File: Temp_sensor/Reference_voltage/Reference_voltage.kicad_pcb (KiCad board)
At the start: 2 copper layers, 100 x 100 mm, 58 parts, among them J1 CN3, J2 CN4, SW1 SW_DIP_x01, SW2 SW_DIP_x01, U1 HDSP-7401_Paulo, U2 HDSP-7401_Paulo, U3 HDSP-7401_Paulo, U4 HDSP-7401_Paulo, U5 LM4128, U6 74HC595, U7 74HC595, U8 74HC595, U9 74HC595

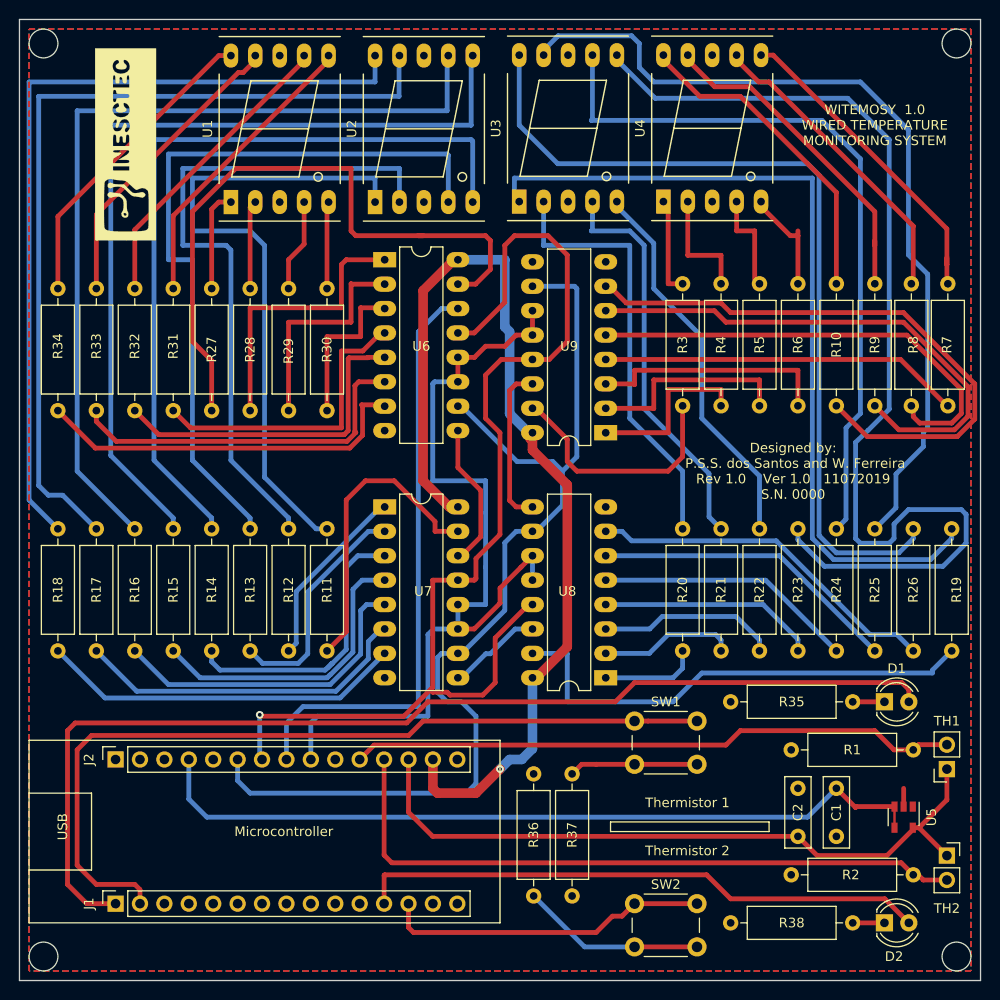
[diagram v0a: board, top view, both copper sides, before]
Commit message: Through Hole to SMD components
first print of the board
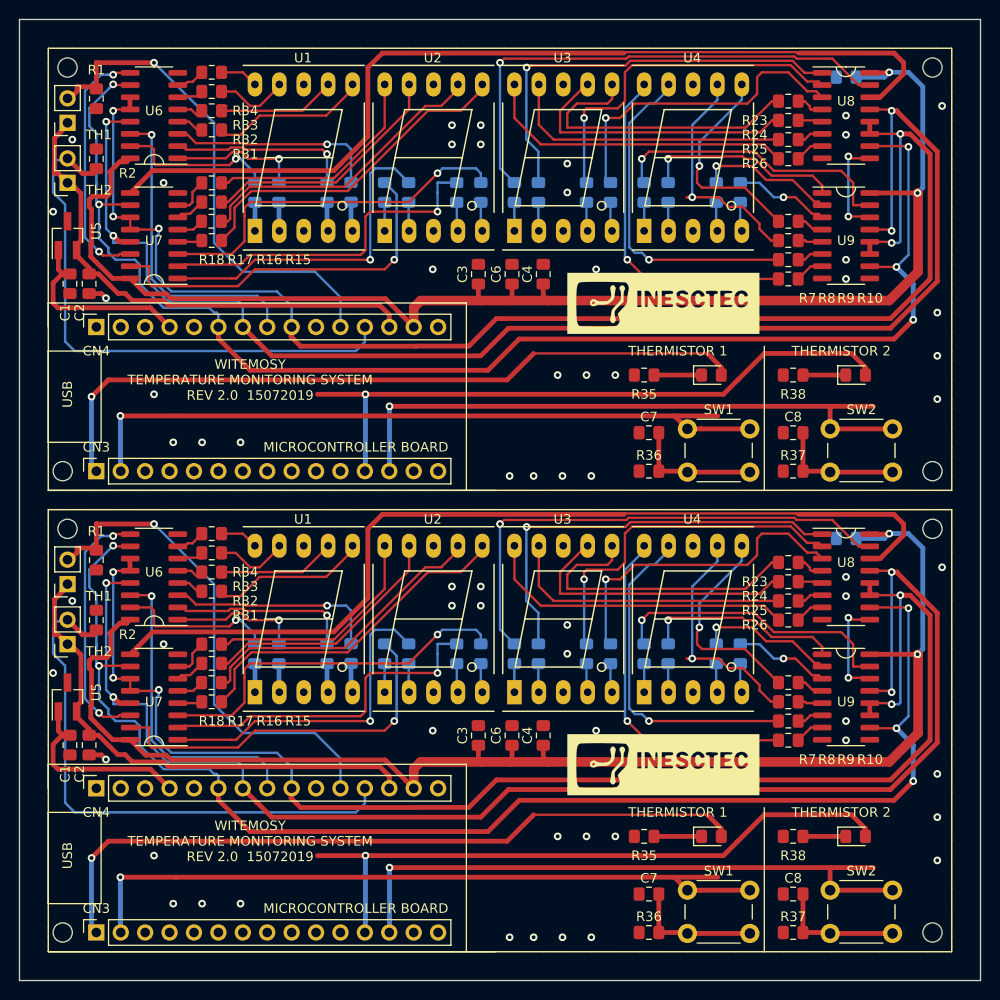
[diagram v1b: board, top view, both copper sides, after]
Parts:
- removed the C1 at (180.0, 125.0)
- removed the C2 at (176.0, 130.0)
- removed D1, D2: LED, LED_THT:LED_D4.0mm
- removed the G*** at (106.0, 58.0)
- removed J1: CN3, Connector_PinSocket_2.54mm:PinSocket_1x15_P2.54mm_Vertical
- removed J2: CN4, Connector_PinSocket_2.54mm:PinSocket_1x15_P2.54mm_Vertical
- removed the R1 at (188.0, 121.0)
- removed the R10 at (180.0, 72.5)
- removed the R11 at (127.0, 98.0)
- removed the R12 at (123.0, 98.0)
- removed the R13 at (119.0, 98.0)
- removed the R14 at (115.0, 98.0)
- removed the R15 at (111.0, 98.0)
- removed the R16 at (107.0, 98.0)
- removed the R17 at (103.0, 98.0)
- removed the R18 at (99.0, 98.0)
- removed the R19 at (192.0, 98.0)
- removed the R2 at (188.0, 134.0)
- removed the R20 at (164.0, 98.0)
- removed the R21 at (168.0, 98.0)
- removed the R22 at (172.0, 98.0)
- removed the R23 at (176.0, 98.0)
- removed the R24 at (180.0, 98.0)
- removed the R25 at (184.0, 98.0)
- removed the R26 at (188.0, 98.0)
- removed the R27 at (115.0, 73.0)
- removed the R28 at (119.0, 73.0)
- removed the R29 at (123.0, 73.0)
- removed the R3 at (164.0, 72.5)
- removed the R30 at (127.0, 73.0)
- removed the R31 at (111.0, 73.0)
- removed the R32 at (107.0, 73.0)
- removed the R33 at (103.0, 73.0)
- removed the R34 at (99.0, 73.0)
- removed the R35 at (169.0, 116.0)
- removed the R36 at (152.5, 136.2)
- removed the R37 at (148.5, 123.5)
- removed the R38 at (169.0, 139.0)
- removed the R4 at (168.0, 72.5)
- removed the R5 at (172.0, 72.5)
- removed the R6 at (176.0, 72.5)
- removed the R7 at (191.6, 72.5)
- removed the R8 at (187.8, 72.5)
- removed the R9 at (184.0, 72.5)
- removed the SW1 at (159.0, 118.0)
- removed the SW2 at (159.0, 137.0)
- removed the TH1 at (191.5, 123.0)
- removed the TH2 at (191.5, 132.0)
- removed the U1 at (117.0, 64.0)
- removed the U2 at (132.0, 64.0)
- removed the U3 at (147.0, 64.0)
- removed the U4 at (162.0, 64.0)
- removed the U5 at (187.0, 128.0)
- removed the U6 at (133.0, 70.0)
- removed the U7 at (133.0, 95.7)
- removed the U8 at (156.0, 113.5)
- removed the U9 at (156.0, 88.0)
- added C1: 100n, Capacitor_SMD:C_0805_2012Metric_Pad1.15x1.40mm_HandSolder, F.Cu at (100.2, 120.5)
- added C1: 100n, Capacitor_SMD:C_0805_2012Metric_Pad1.15x1.40mm_HandSolder, F.Cu at (100.2, 72.5)
- added C2: 100n, Capacitor_SMD:C_0805_2012Metric_Pad1.15x1.40mm_HandSolder, F.Cu at (102.2, 120.5)
- added C2: 100n, Capacitor_SMD:C_0805_2012Metric_Pad1.15x1.40mm_HandSolder, F.Cu at (102.2, 72.5)
- added C3: 100n, Capacitor_SMD:C_0805_2012Metric_Pad1.15x1.40mm_HandSolder, F.Cu at (142.8, 119.5)
- added C3: 100n, Capacitor_SMD:C_0805_2012Metric_Pad1.15x1.40mm_HandSolder, F.Cu at (142.8, 71.5)
- added C4: 100n, Capacitor_SMD:C_0805_2012Metric_Pad1.15x1.40mm_HandSolder, F.Cu at (149.5, 119.5)
- added C4: 100n, Capacitor_SMD:C_0805_2012Metric_Pad1.15x1.40mm_HandSolder, F.Cu at (149.5, 71.5)
- added C5: 100n, Capacitor_SMD:C_0805_2012Metric_Pad1.15x1.40mm_HandSolder, B.Cu at (181.0, 99.0)
- added C5: 100n, Capacitor_SMD:C_0805_2012Metric_Pad1.15x1.40mm_HandSolder, B.Cu at (181.0, 51.0)
- added C6: 100n, Capacitor_SMD:C_0805_2012Metric_Pad1.15x1.40mm_HandSolder, F.Cu at (146.2, 119.5)
- added C6: 100n, Capacitor_SMD:C_0805_2012Metric_Pad1.15x1.40mm_HandSolder, F.Cu at (146.2, 71.5)
- added C7: 100n, Capacitor_SMD:C_0805_2012Metric_Pad1.15x1.40mm_HandSolder, F.Cu at (160.5, 136.0)
- added C7: 100n, Capacitor_SMD:C_0805_2012Metric_Pad1.15x1.40mm_HandSolder, F.Cu at (160.5, 88.0)
- added C8: 100n, Capacitor_SMD:C_0805_2012Metric_Pad1.15x1.40mm_HandSolder, F.Cu at (175.5, 136.0)
- added C8: 100n, Capacitor_SMD:C_0805_2012Metric_Pad1.15x1.40mm_HandSolder, F.Cu at (175.5, 88.0)
- added CN3: CN3, Connector_PinSocket_2.54mm:PinSocket_1x15_P2.54mm_Vertical, F.Cu at (103.0, 140.0)
- added CN3: CN3, Connector_PinSocket_2.54mm:PinSocket_1x15_P2.54mm_Vertical, F.Cu at (103.0, 92.0)
- added CN4: CN4, Connector_PinSocket_2.54mm:PinSocket_1x15_P2.54mm_Vertical, F.Cu at (103.0, 125.0)
- added CN4: CN4, Connector_PinSocket_2.54mm:PinSocket_1x15_P2.54mm_Vertical, F.Cu at (103.0, 77.0)
- added G***: LOGO, Documents:logoinesc4, F.Cu at (162.0, 122.5)
- added G***: LOGO, Documents:logoinesc4, F.Cu at (162.0, 74.5)
- added ON: LED, LED_SMD:LED_0805_2012Metric_Pad1.15x1.40mm_HandSolder, F.Cu at (182.0, 130.0)
- added ON: LED, LED_SMD:LED_0805_2012Metric_Pad1.15x1.40mm_HandSolder, F.Cu at (167.0, 130.0)
- added ON: LED, LED_SMD:LED_0805_2012Metric_Pad1.15x1.40mm_HandSolder, F.Cu at (182.0, 82.0)
- added ON: LED, LED_SMD:LED_0805_2012Metric_Pad1.15x1.40mm_HandSolder, F.Cu at (167.0, 82.0)
- added R1: 10k, Resistor_SMD:R_0805_2012Metric_Pad1.15x1.40mm_HandSolder, F.Cu at (103.0, 101.2)
- added R1: 10k, Resistor_SMD:R_0805_2012Metric_Pad1.15x1.40mm_HandSolder, F.Cu at (103.0, 53.2)
- added R10: 560, Resistor_SMD:R_0805_2012Metric_Pad1.15x1.40mm_HandSolder, F.Cu at (175.0, 120.0)
- added R10: 560, Resistor_SMD:R_0805_2012Metric_Pad1.15x1.40mm_HandSolder, F.Cu at (175.0, 72.0)
- added R11: 560, Resistor_SMD:R_0805_2012Metric_Pad1.15x1.40mm_HandSolder, B.Cu at (133.0, 111.0)
- added R11: 560, Resistor_SMD:R_0805_2012Metric_Pad1.15x1.40mm_HandSolder, B.Cu at (133.0, 63.0)
- added R12: 560, Resistor_SMD:R_0805_2012Metric_Pad1.15x1.40mm_HandSolder, B.Cu at (135.5, 111.0)
- added R12: 560, Resistor_SMD:R_0805_2012Metric_Pad1.15x1.40mm_HandSolder, B.Cu at (135.5, 63.0)
- added R13: 560, Resistor_SMD:R_0805_2012Metric_Pad1.15x1.40mm_HandSolder, B.Cu at (140.5, 111.0)
- added R13: 560, Resistor_SMD:R_0805_2012Metric_Pad1.15x1.40mm_HandSolder, B.Cu at (140.5, 63.0)
- added R14: 560, Resistor_SMD:R_0805_2012Metric_Pad1.15x1.40mm_HandSolder, B.Cu at (143.0, 111.0)
- added R14: 560, Resistor_SMD:R_0805_2012Metric_Pad1.15x1.40mm_HandSolder, B.Cu at (143.0, 63.0)
- added R15: 560, Resistor_SMD:R_0805_2012Metric_Pad1.15x1.40mm_HandSolder, F.Cu at (115.0, 116.0)
- added R15: 560, Resistor_SMD:R_0805_2012Metric_Pad1.15x1.40mm_HandSolder, F.Cu at (115.0, 68.0)
- added R16: 560, Resistor_SMD:R_0805_2012Metric_Pad1.15x1.40mm_HandSolder, F.Cu at (115.0, 114.0)
- added R16: 560, Resistor_SMD:R_0805_2012Metric_Pad1.15x1.40mm_HandSolder, F.Cu at (115.0, 66.0)
- added R17: 560, Resistor_SMD:R_0805_2012Metric_Pad1.15x1.40mm_HandSolder, F.Cu at (115.0, 112.0)
- added R17: 560, Resistor_SMD:R_0805_2012Metric_Pad1.15x1.40mm_HandSolder, F.Cu at (115.0, 64.0)
- added R18: 560, Resistor_SMD:R_0805_2012Metric_Pad1.15x1.40mm_HandSolder, F.Cu at (115.0, 110.0)
- added R18: 560, Resistor_SMD:R_0805_2012Metric_Pad1.15x1.40mm_HandSolder, F.Cu at (115.0, 62.0)
- added R19: 560, Resistor_SMD:R_0805_2012Metric_Pad1.15x1.40mm_HandSolder, B.Cu at (146.5, 111.0)
- added R19: 560, Resistor_SMD:R_0805_2012Metric_Pad1.15x1.40mm_HandSolder, B.Cu at (146.5, 63.0)
- added R2: 10k, Resistor_SMD:R_0805_2012Metric_Pad1.15x1.40mm_HandSolder, F.Cu at (103.0, 107.5)
- added R2: 10k, Resistor_SMD:R_0805_2012Metric_Pad1.15x1.40mm_HandSolder, F.Cu at (103.0, 59.5)
- added R20: 560, Resistor_SMD:R_0805_2012Metric_Pad1.15x1.40mm_HandSolder, B.Cu at (149.0, 111.0)
- added R20: 560, Resistor_SMD:R_0805_2012Metric_Pad1.15x1.40mm_HandSolder, B.Cu at (149.0, 63.0)
- added R21: 560, Resistor_SMD:R_0805_2012Metric_Pad1.15x1.40mm_HandSolder, B.Cu at (154.0, 111.0)
- added R21: 560, Resistor_SMD:R_0805_2012Metric_Pad1.15x1.40mm_HandSolder, B.Cu at (154.0, 63.0)
- added R22: 560, Resistor_SMD:R_0805_2012Metric_Pad1.15x1.40mm_HandSolder, B.Cu at (156.5, 111.0)
- added R22: 560, Resistor_SMD:R_0805_2012Metric_Pad1.15x1.40mm_HandSolder, B.Cu at (156.5, 63.0)
- added R23: 560, Resistor_SMD:R_0805_2012Metric_Pad1.15x1.40mm_HandSolder, F.Cu at (175.0, 101.5)
- added R23: 560, Resistor_SMD:R_0805_2012Metric_Pad1.15x1.40mm_HandSolder, F.Cu at (175.0, 53.5)
- added R24: 560, Resistor_SMD:R_0805_2012Metric_Pad1.15x1.40mm_HandSolder, F.Cu at (175.0, 103.5)
- added R24: 560, Resistor_SMD:R_0805_2012Metric_Pad1.15x1.40mm_HandSolder, F.Cu at (175.0, 55.5)
- added R25: 560, Resistor_SMD:R_0805_2012Metric_Pad1.15x1.40mm_HandSolder, F.Cu at (175.0, 105.5)
- added R25: 560, Resistor_SMD:R_0805_2012Metric_Pad1.15x1.40mm_HandSolder, F.Cu at (175.0, 57.5)
- added R26: 560, Resistor_SMD:R_0805_2012Metric_Pad1.15x1.40mm_HandSolder, F.Cu at (175.0, 107.5)
- added R26: 560, Resistor_SMD:R_0805_2012Metric_Pad1.15x1.40mm_HandSolder, F.Cu at (175.0, 59.5)
- added R27: 560, Resistor_SMD:R_0805_2012Metric_Pad1.15x1.40mm_HandSolder, B.Cu at (119.5, 111.0)
- added R27: 560, Resistor_SMD:R_0805_2012Metric_Pad1.15x1.40mm_HandSolder, B.Cu at (119.5, 63.0)
- added R28: 560, Resistor_SMD:R_0805_2012Metric_Pad1.15x1.40mm_HandSolder, B.Cu at (122.0, 111.0)
- added R28: 560, Resistor_SMD:R_0805_2012Metric_Pad1.15x1.40mm_HandSolder, B.Cu at (122.0, 63.0)
- added R29: 560, Resistor_SMD:R_0805_2012Metric_Pad1.15x1.40mm_HandSolder, B.Cu at (127.0, 111.0)
- added R29: 560, Resistor_SMD:R_0805_2012Metric_Pad1.15x1.40mm_HandSolder, B.Cu at (127.0, 63.0)
- added R3: 560, Resistor_SMD:R_0805_2012Metric_Pad1.15x1.40mm_HandSolder, B.Cu at (160.0, 111.0)
- added R3: 560, Resistor_SMD:R_0805_2012Metric_Pad1.15x1.40mm_HandSolder, B.Cu at (160.0, 63.0)
- added R30: 560, Resistor_SMD:R_0805_2012Metric_Pad1.15x1.40mm_HandSolder, B.Cu at (129.5, 111.0)
- added R30: 560, Resistor_SMD:R_0805_2012Metric_Pad1.15x1.40mm_HandSolder, B.Cu at (129.5, 63.0)
- added R31: 560, Resistor_SMD:R_0805_2012Metric_Pad1.15x1.40mm_HandSolder, F.Cu at (115.0, 104.5)
- added R31: 560, Resistor_SMD:R_0805_2012Metric_Pad1.15x1.40mm_HandSolder, F.Cu at (115.0, 56.5)
- added R32: 560, Resistor_SMD:R_0805_2012Metric_Pad1.15x1.40mm_HandSolder, F.Cu at (115.0, 102.5)
- added R32: 560, Resistor_SMD:R_0805_2012Metric_Pad1.15x1.40mm_HandSolder, F.Cu at (115.0, 54.5)
- added R33: 560, Resistor_SMD:R_0805_2012Metric_Pad1.15x1.40mm_HandSolder, F.Cu at (115.0, 100.5)
- added R33: 560, Resistor_SMD:R_0805_2012Metric_Pad1.15x1.40mm_HandSolder, F.Cu at (115.0, 52.5)
- added R34: 560, Resistor_SMD:R_0805_2012Metric_Pad1.15x1.40mm_HandSolder, F.Cu at (115.0, 98.5)
- added R34: 560, Resistor_SMD:R_0805_2012Metric_Pad1.15x1.40mm_HandSolder, F.Cu at (115.0, 50.5)
- added R35: 220, Resistor_SMD:R_0805_2012Metric_Pad1.15x1.40mm_HandSolder, F.Cu at (160.0, 130.0)
- added R35: 220, Resistor_SMD:R_0805_2012Metric_Pad1.15x1.40mm_HandSolder, F.Cu at (160.0, 82.0)
- added R36: 1k, Resistor_SMD:R_0805_2012Metric_Pad1.15x1.40mm_HandSolder, F.Cu at (160.5, 140.0)
- added R36: 1k, Resistor_SMD:R_0805_2012Metric_Pad1.15x1.40mm_HandSolder, F.Cu at (160.5, 92.0)
- added R37: 1k, Resistor_SMD:R_0805_2012Metric_Pad1.15x1.40mm_HandSolder, F.Cu at (175.5, 140.0)
- added R37: 1k, Resistor_SMD:R_0805_2012Metric_Pad1.15x1.40mm_HandSolder, F.Cu at (175.5, 92.0)
- added R38: 220, Resistor_SMD:R_0805_2012Metric_Pad1.15x1.40mm_HandSolder, F.Cu at (175.5, 130.0)
- added R38: 220, Resistor_SMD:R_0805_2012Metric_Pad1.15x1.40mm_HandSolder, F.Cu at (175.5, 82.0)
- added R4: 560, Resistor_SMD:R_0805_2012Metric_Pad1.15x1.40mm_HandSolder, B.Cu at (162.5, 111.0)
- added R4: 560, Resistor_SMD:R_0805_2012Metric_Pad1.15x1.40mm_HandSolder, B.Cu at (162.5, 63.0)
- added R5: 560, Resistor_SMD:R_0805_2012Metric_Pad1.15x1.40mm_HandSolder, B.Cu at (167.5, 111.0)
- added R5: 560, Resistor_SMD:R_0805_2012Metric_Pad1.15x1.40mm_HandSolder, B.Cu at (167.5, 63.0)
- added R6: 560, Resistor_SMD:R_0805_2012Metric_Pad1.15x1.40mm_HandSolder, B.Cu at (170.0, 111.0)
- added R6: 560, Resistor_SMD:R_0805_2012Metric_Pad1.15x1.40mm_HandSolder, B.Cu at (170.0, 63.0)
- added R7: 560, Resistor_SMD:R_0805_2012Metric_Pad1.15x1.40mm_HandSolder, F.Cu at (175.0, 114.0)
- added R7: 560, Resistor_SMD:R_0805_2012Metric_Pad1.15x1.40mm_HandSolder, F.Cu at (175.0, 66.0)
- added R8: 560, Resistor_SMD:R_0805_2012Metric_Pad1.15x1.40mm_HandSolder, F.Cu at (175.0, 116.0)
- added R8: 560, Resistor_SMD:R_0805_2012Metric_Pad1.15x1.40mm_HandSolder, F.Cu at (175.0, 68.0)
- added R9: 560, Resistor_SMD:R_0805_2012Metric_Pad1.15x1.40mm_HandSolder, F.Cu at (175.0, 118.0)
- added R9: 560, Resistor_SMD:R_0805_2012Metric_Pad1.15x1.40mm_HandSolder, F.Cu at (175.0, 70.0)
- added SW1: SW_DIP_x01, Button_Switch_THT:SW_PUSH_6mm_H5mm, F.Cu at (164.5, 135.6)
- added SW1: SW_DIP_x01, Button_Switch_THT:SW_PUSH_6mm_H5mm, F.Cu at (164.5, 87.6)
- added SW2: SW_DIP_x01, Button_Switch_THT:SW_PUSH_6mm_H5mm, F.Cu at (179.3, 135.6)
- added SW2: SW_DIP_x01, Button_Switch_THT:SW_PUSH_6mm_H5mm, F.Cu at (179.3, 87.6)
- added TH1: Thermistor_NTC, Connector_PinSocket_2.54mm:PinSocket_1x02_P2.54mm_Vertical, F.Cu at (100.0, 103.8)
- added TH1: Thermistor_NTC, Connector_PinSocket_2.54mm:PinSocket_1x02_P2.54mm_Vertical, F.Cu at (100.0, 55.8)
- added TH2: Thermistor_NTC, Connector_PinSocket_2.54mm:PinSocket_1x02_P2.54mm_Vertical, F.Cu at (100.0, 110.0)
- added TH2: Thermistor_NTC, Connector_PinSocket_2.54mm:PinSocket_1x02_P2.54mm_Vertical, F.Cu at (100.0, 62.0)
- added U1: HDSP-7401_Paulo, Display_7Segment:7SegmentLED_LTS6760_LTS6780, F.Cu at (119.5, 115.0)
- added U1: HDSP-7401_Paulo, Display_7Segment:7SegmentLED_LTS6760_LTS6780, F.Cu at (119.5, 67.0)
- added U2: HDSP-7401_Paulo, Display_7Segment:7SegmentLED_LTS6760_LTS6780, F.Cu at (133.0, 115.0)
- added U2: HDSP-7401_Paulo, Display_7Segment:7SegmentLED_LTS6760_LTS6780, F.Cu at (133.0, 67.0)
- added U3: HDSP-7401_Paulo, Display_7Segment:7SegmentLED_LTS6760_LTS6780, F.Cu at (146.5, 115.0)
- added U3: HDSP-7401_Paulo, Display_7Segment:7SegmentLED_LTS6760_LTS6780, F.Cu at (146.5, 67.0)
- added U4: HDSP-7401_Paulo, Display_7Segment:7SegmentLED_LTS6760_LTS6780, F.Cu at (160.0, 115.0)
- added U4: HDSP-7401_Paulo, Display_7Segment:7SegmentLED_LTS6760_LTS6780, F.Cu at (160.0, 67.0)
- added U5: REF3033, Package_TO_SOT_SMD:SOT-23_Handsoldering, F.Cu at (100.0, 115.5)
- added U5: REF3033, Package_TO_SOT_SMD:SOT-23_Handsoldering, F.Cu at (100.0, 67.5)
- added U6: 74HC595, Package_SO:SOIC-16_3.9x9.9mm_P1.27mm, F.Cu at (109.0, 103.0)
- added U6: 74HC595, Package_SO:SOIC-16_3.9x9.9mm_P1.27mm, F.Cu at (109.0, 55.0)
- added U7: 74HC595, Package_SO:SOIC-16_3.9x9.9mm_P1.27mm, F.Cu at (109.0, 115.5)
- added U7: 74HC595, Package_SO:SOIC-16_3.9x9.9mm_P1.27mm, F.Cu at (109.0, 67.5)
- added U8: 74HC595, Package_SO:SOIC-16_3.9x9.9mm_P1.27mm, F.Cu at (181.0, 103.0)
- added U8: 74HC595, Package_SO:SOIC-16_3.9x9.9mm_P1.27mm, F.Cu at (181.0, 55.0)
- added U9: 74HC595, Package_SO:SOIC-16_3.9x9.9mm_P1.27mm, F.Cu at (181.0, 115.5)
- added U9: 74HC595, Package_SO:SOIC-16_3.9x9.9mm_P1.27mm, F.Cu at (181.0, 67.5)
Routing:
- net /PA4_CLK: track 93.3 -> 303.3 mm, vias 0 -> 10
- net V3.3: track 106.0 -> 292.2 mm, vias 1 -> 4
- net /PA6_OE: track 119.2 -> 303.7 mm, vias 1 -> 8
- net Net-(U7-Pad9): track 9.86 -> 193.8 mm
- net /PA7_CLR: track 110.1 -> 288.7 mm, vias 0 -> 10
- net /PA10_SW2: track 34.0 -> 131.9 mm, vias 0 -> 2
- net Net-(R19-Pad1): track 88.3 -> 5.95 mm
- net Net-(R20-Pad2): track 10.2 -> 88.4 mm, vias 0 -> 2
- net /PA8_LD2: track 59.6 -> 136.4 mm, vias 0 -> 2
- net Net-(R14-Pad1): track 82.6 -> 6.08 mm
- net Net-(R13-Pad1): track 78.0 -> 6.05 mm
- net /PA10_SW1: track 86.8 -> 152.7 mm, vias 0 -> 2
- net Net-(R12-Pad1): track 70.7 -> 5.98 mm
- net Net-(R11-Pad1): track 68.0 -> 5.95 mm
- net Net-(R21-Pad2): track 14.2 -> 73.9 mm, vias 0 -> 2
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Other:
- outline, holes or cut-outs redrawn
- board text added: "MICROCONTROLLER BOARD"
- board text added: "P. S. S. dos Santos W. Ferreira"
- board text added: "SAFEWATER"
- board text added: "THERMISTOR 1"
- board text added: "THERMISTOR 2"
- board text added: "WITEMOSY TEMPERATURE MONITORING SYSTEM REV 2.0 15072019"
- board text removed: "Designed by: P.S.S. dos Santos and W. Ferreira Rev 1.0 Ver 1.0 11072019 S.N. 0000"
- board text removed: "Microcontroller"
- board text removed: "Thermistor 1"
- board text removed: "Thermistor 2"
- board text removed: "WITEMOSY 1.0 WIRED TEMPERATURE MONITORING SYSTEM"
